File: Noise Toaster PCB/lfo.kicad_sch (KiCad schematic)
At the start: 20 parts, among them U2 LM324

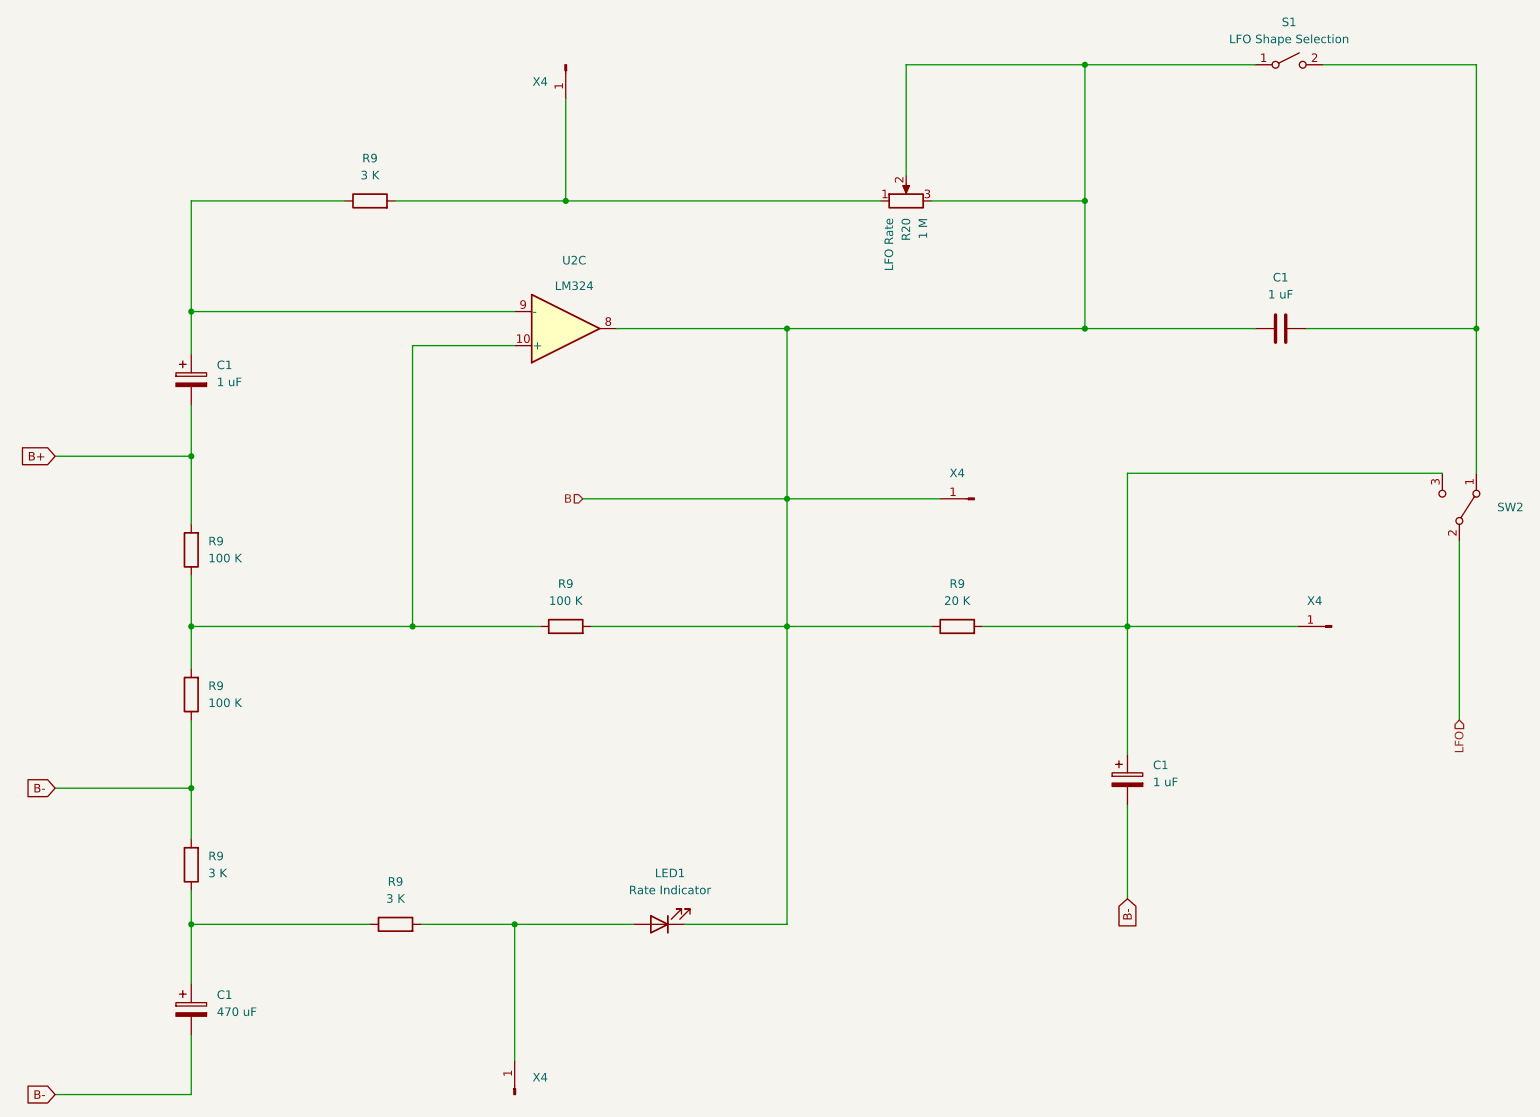
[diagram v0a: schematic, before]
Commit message: updated schematics
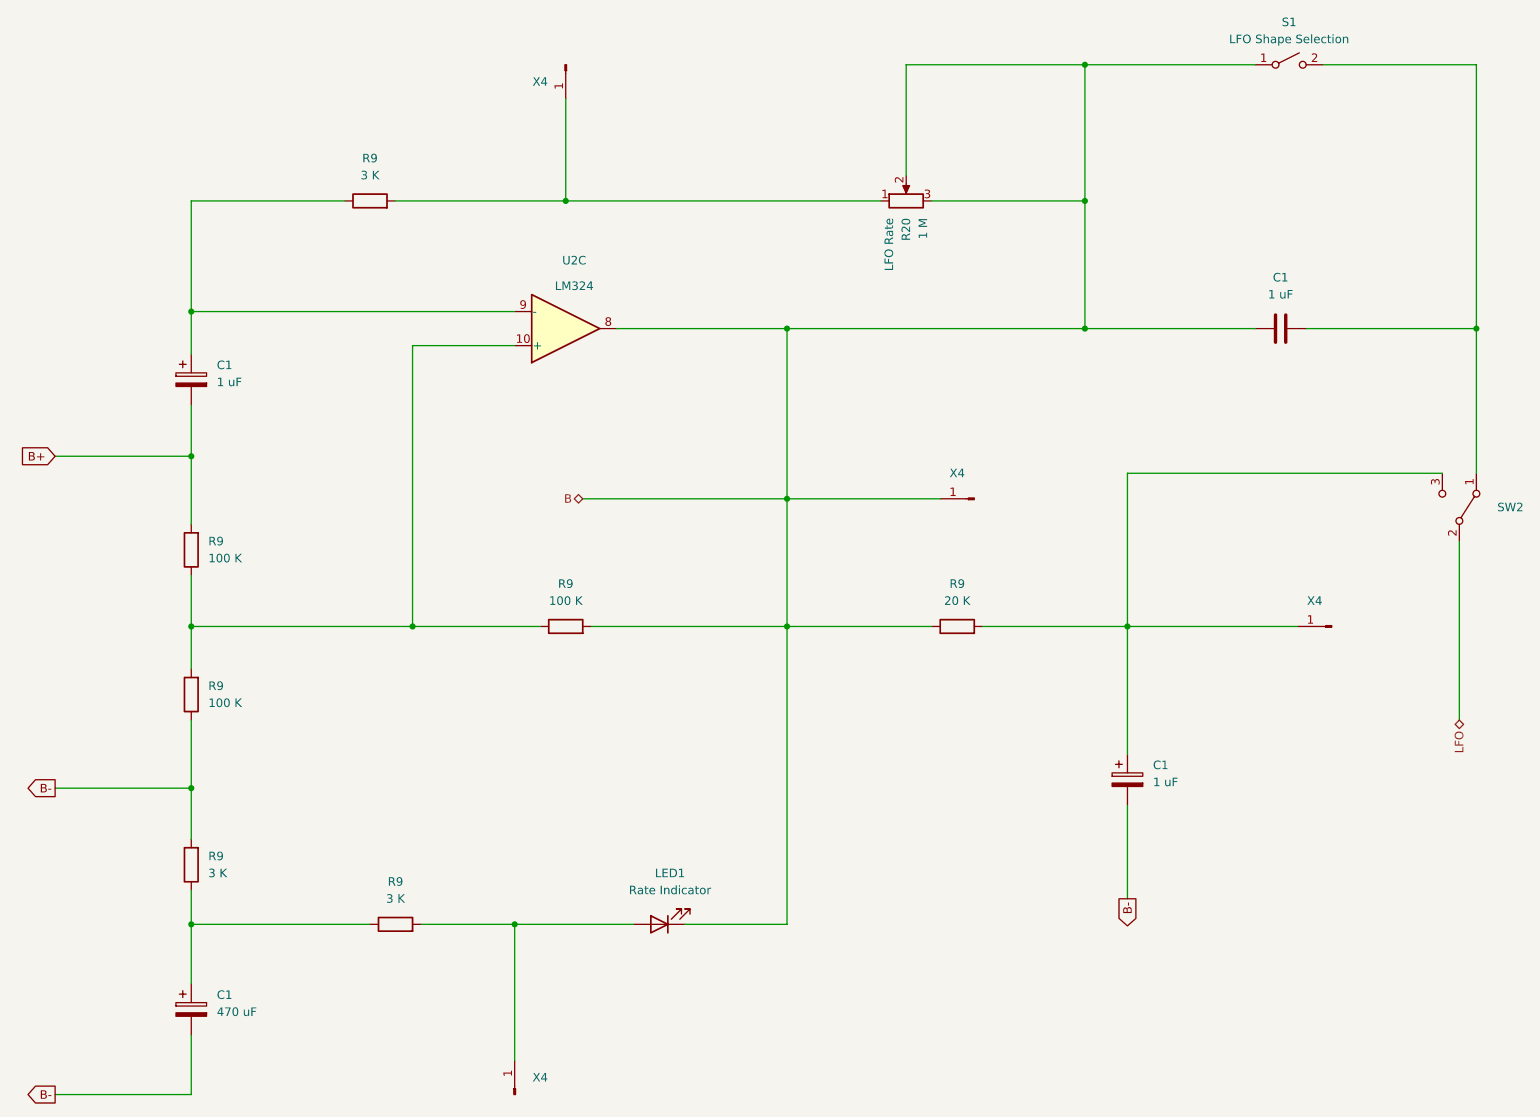
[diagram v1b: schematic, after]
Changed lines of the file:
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@@
     (stroke (width 0) (type default))
   )
-  (global_label "B-" (shape input) (at 43.18 132.08 180) (fields_autoplaced)
+  (global_label "B-" (shape output) (at 43.18 132.08 180) (fields_autoplaced)
     (effects (font (size 1.27 1.27)) (justify right))
     (property "Intersheetrefs" "${INTERSHEET_REFS}" (at 37.3524 132.08 0)
@@
     )
   )
-  (global_label "B-" (shape input) (at 203.2 148.59 270) (fields_autoplaced)
+  (global_label "B-" (shape output) (at 203.2 148.59 270) (fields_autoplaced)
     (effects (font (size 1.27 1.27)) (justify right))
     (property "Intersheetrefs" "${INTERSHEET_REFS}" (at 203.2 154.4176 90)
@@
     )
   )
-  (global_label "B-" (shape input) (at 43.18 177.8 180) (fields_autoplaced)
+  (global_label "B-" (shape output) (at 43.18 177.8 180) (fields_autoplaced)
     (effects (font (size 1.27 1.27)) (justify right))
     (property "Intersheetrefs" "${INTERSHEET_REFS}" (at 37.3524 177.8 0)
@@
     )
   )
-  (hierarchical_label "B" (shape input) (at 121.92 88.9 180) (fields_autoplaced)
+  (hierarchical_label "B" (shape bidirectional) (at 121.92 88.9 180) (fields_autoplaced)
     (effects (font (size 1.27 1.27)) (justify right))
   )
-  (hierarchical_label "LFO" (shape input) (at 252.73 121.92 270) (fields_autoplaced)
+  (hierarchical_label "LFO" (shape bidirectional) (at 252.73 121.92 270) (fields_autoplaced)
     (effects (font (size 1.27 1.27)) (justify right))
   )

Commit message: refactored the schematic
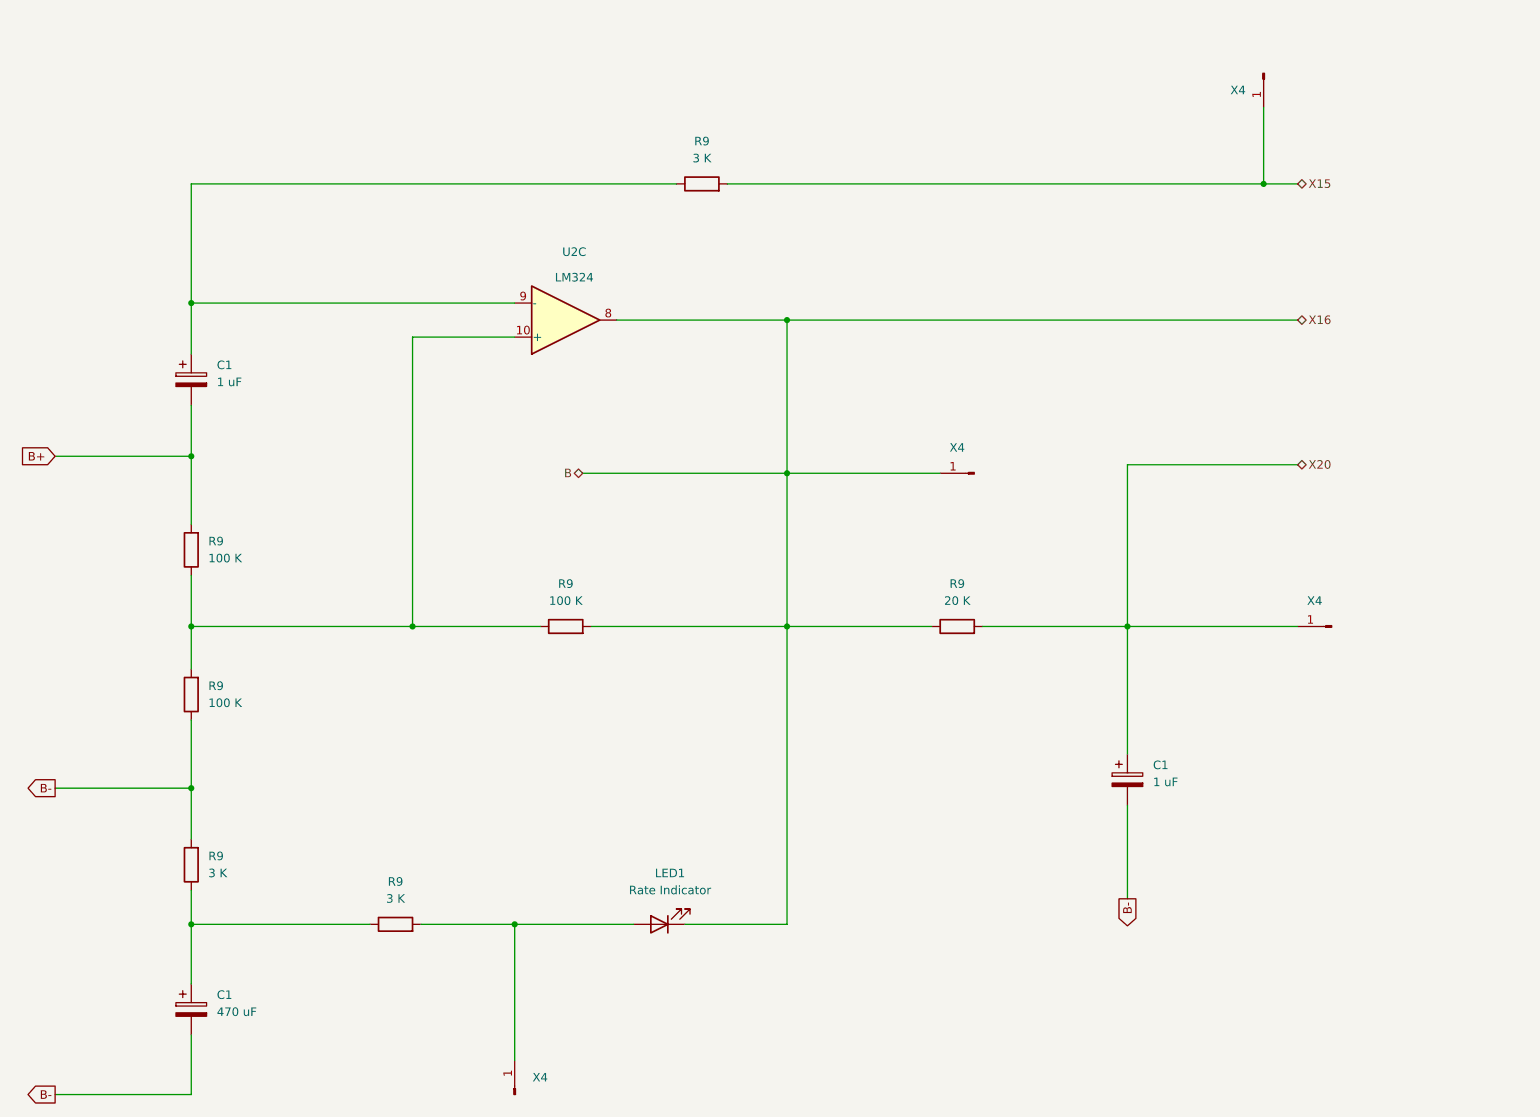
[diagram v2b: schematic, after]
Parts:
- removed C1: 1 uF, symbol Device:C
- removed R20: 1 M, symbol Device:R_Potentiometer
- removed S1: LFO Shape Selection, symbol Switch:SW_SPST
- removed SW2: ~, symbol Switch:SW_SPDT
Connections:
- net X20: now reaches C1.1, R9.2, X4.1 (Pin_1)
- net X15: now reaches R9.2, X4.1 (Pin_1)
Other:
- moved on the sheet: R9, U2C, X4
